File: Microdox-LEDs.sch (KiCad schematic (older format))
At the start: 33 parts, among them P1 USB, P2 CONN_01X03, SW0:0 SWITCH_DIODE, SW0:1 SWITCH_DIODE, SW0:2 SWITCH_DIODE, SW0:3 SWITCH_DIODE, SW0:4 SWITCH_DIODE, SW0:5 SWITCH_DIODE, SW0:6 SWITCH_DIODE, SW1:0 SWITCH_DIODE, SW1:1 SWITCH_DIODE, SW1:2 SWITCH_DIODE, SW1:3 SWITCH_DIODE, SW1:4 SWITCH_DIODE, SW1:5 SWITCH_DIODE, SW2:0 SWITCH_DIODE, SW2:1 SWITCH_DIODE, SW2:2 SWITCH_DIODE, SW2:3 SWITCH_DIODE, SW2:4 SWITCH_DIODE, SW2:5 SWITCH_DIODE, SW2:6 SWITCH_DIODE, SW3:0 SWITCH_DIODE, SW3:1 SWITCH_DIODE, SW3:2 SWITCH_DIODE, SW3:3 SWITCH_DIODE, SW3:4 SWITCH_DIODE, SW3:5 SWITCH_DIODE, SW3:6 SWITCH_DIODE, SW4:5 SWITCH_DIODE, SW4:6 SWITCH_DIODE

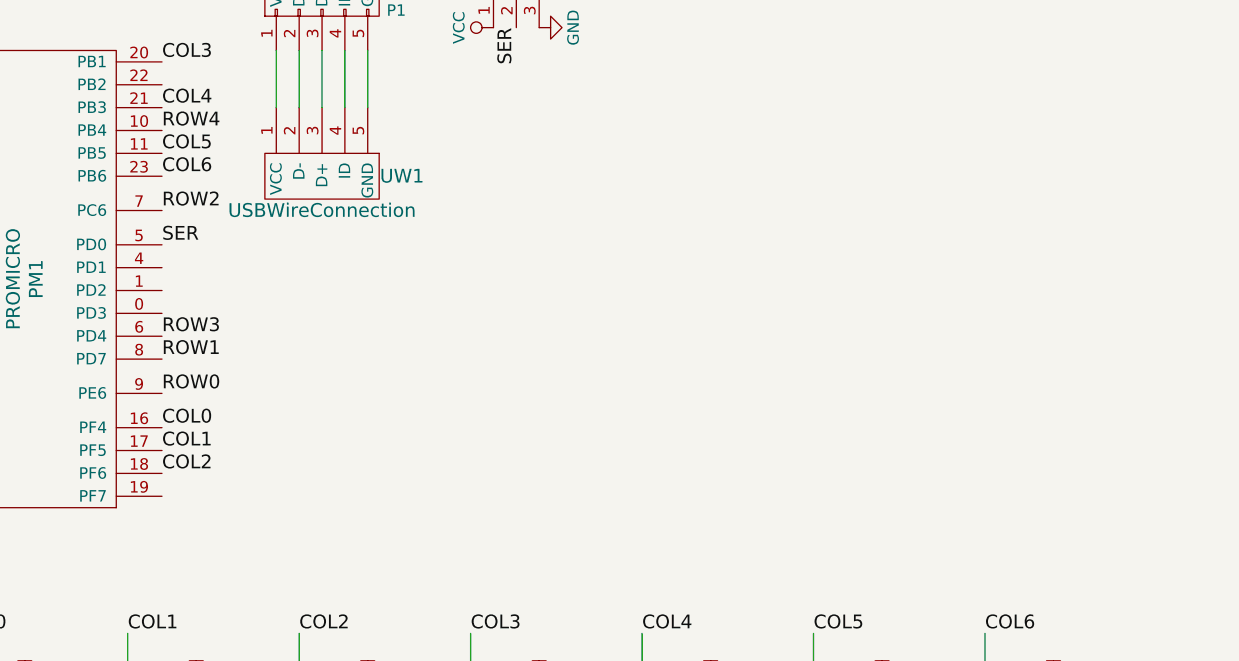
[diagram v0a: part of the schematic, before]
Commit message: Add version without backlighting
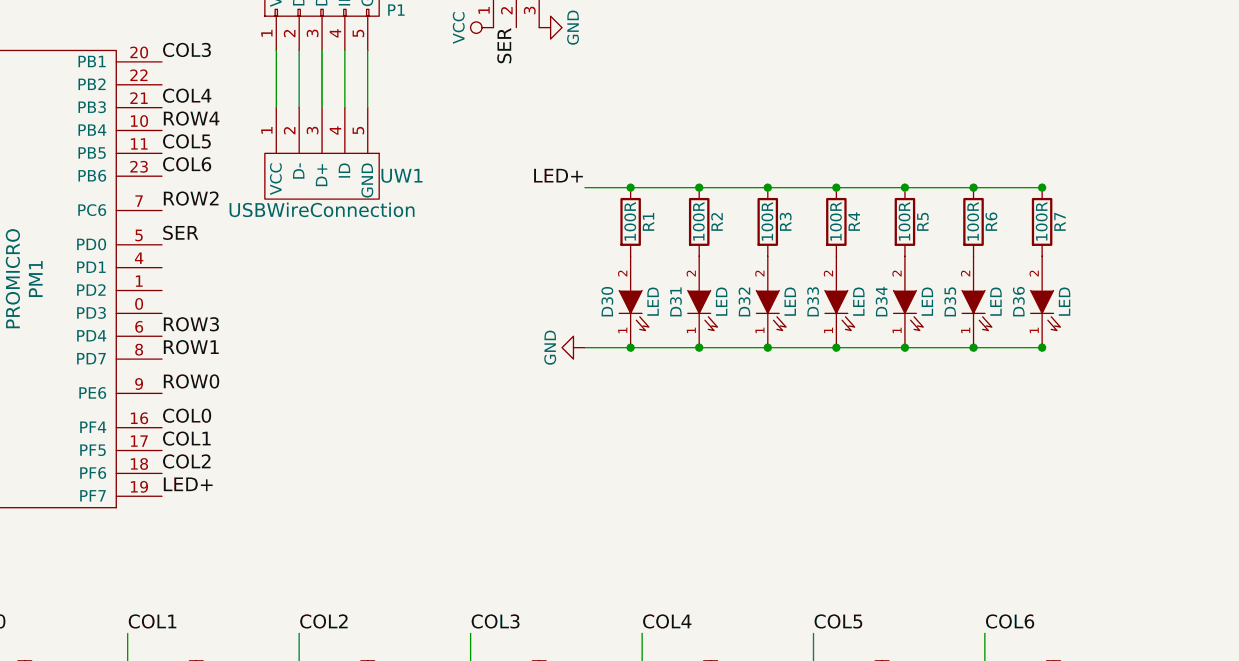
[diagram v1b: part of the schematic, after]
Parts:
- added D30, D31, D32, D33, D34, D35, D36: LED, LEDs:LED_1206, symbol LED
- added R1, R2, R3, R4, R5, R6, R7: 100R, Resistors_SMD:R_1206_HandSoldering, symbol R
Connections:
- net GND: now also D30.1 (K), D31.1 (K), D32.1 (K), D33.1 (K), D34.1 (K), D35.1 (K), D36.1 (K)
- net LED+: now reaches PM1.19 (PF7)
- net LED+: now also R1.1, R2.1, R3.1, R4.1, R5.1, R6.1, R7.1
- new net: D30.2 (A), R1.2
- new net: D31.2 (A), R2.2
- new net: D32.2 (A), R3.2
- new net: D33.2 (A), R4.2
- new net: D34.2 (A), R5.2
- new net: D35.2 (A), R6.2
- new net: D36.2 (A), R7.2
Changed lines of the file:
@@
 	1    0    0    -1
 $EndComp
+Text Label 2100 3450 0    60   ~ 0
+LED+
+Connection ~ 5050 2800
+Connection ~ 5650 2800
+Connection ~ 5950 2100
+Connection ~ 5650 2100
+Connection ~ 5350 2100
+Connection ~ 5050 2100
+Connection ~ 4750 2100
+Connection ~ 4450 2100
+Connection ~ 4150 2100
+Wire Wire Line
+	3950 2100 5950 2100
+Text Label 3950 2100 2    60   ~ 0
+LED+
+$Comp
+L GND #PWR07
+U 1 1 56F73DF4
+P 3950 2800
+F 0 "#PWR07" H 3950 2550 50  0001 C CNN
+F 1 "GND" H 3950 2650 50  0000 C CNN
+F 2 "" H 3950 2800 50  0000 C CNN
+F 3 "" H 3950 2800 50  0000 C CNN
+	1    3950 2800
+	0    1    1    0
+$EndComp
+Connection ~ 4150 2800
+Connection ~ 4450 2800
+Connection ~ 4750 2800
+Connection ~ 5350 2800
+$Comp
+L LED D34
+U 1 1 56F708E7
+P 5350 2600
+F 0 "D34" H 5350 2700 50  0000 C CNN
+F 1 "LED" H 5350 2500 50  0000 C CNN
+F 2 "LEDs:LED_1206" H 5350 2600 50  0001 C CNN
+F 3 "" H 5350 2600 50  0000 C CNN
+	1    5350 2600
+	0    -1   -1   0
+$EndComp
+$Comp
+L LED D33
+U 1 1 56F6ECAD
+P 5050 2600
+F 0 "D33" H 5050 2700 50  0000 C CNN
+F 1 "LED" H 5050 2500 50  0000 C CNN
+F 2 "LEDs:LED_1206" H 5050 2600 50  0001 C CNN
+F 3 "" H 5050 2600 50  0000 C CNN
+	1    5050 2600
+	0    -1   -1   0
+$EndComp
+$Comp
+L LED D32
+U 1 1 56F6EC9F
+P 4750 2600
+F 0 "D32" H 4750 2700 50  0000 C CNN
+F 1 "LED" H 4750 2500 50  0000 C CNN
+F 2 "LEDs:LED_1206" H 4750 2600 50  0001 C CNN
+F 3 "" H 4750 2600 50  0000 C CNN
+	1    4750 2600
+	0    -1   -1   0
+$EndComp
+$Comp
+L LED D31
+U 1 1 56F6D941
+P 4450 2600
+F 0 "D31" H 4450 2700 50  0000 C CNN
+F 1 "LED" H 4450 2500 50  0000 C CNN
+F 2 "LEDs:LED_1206" H 4450 2600 50  0001 C CNN
+F 3 "" H 4450 2600 50  0000 C CNN
+	1    4450 2600
+	0    -1   -1   0
+$EndComp
+$Comp
+L LED D30
+U 1 1 56F68FA0
+P 4150 2600
+F 0 "D30" H 4150 2700 50  0000 C CNN
+F 1 "LED" H 4150 2500 50  0000 C CNN
+F 2 "LEDs:LED_1206" H 4150 2600 50  0001 C CNN
+F 3 "" H 4150 2600 50  0000 C CNN
+	1    4150 2600
+	0    -1   -1   0
+$EndComp
+$Comp
+L R R1
+U 1 1 56F6BB88
+P 4150 2250
+F 0 "R1" V 4230 2250 50  0000 C CNN
+F 1 "100R" V 4150 2250 50  0000 C CNN
+F 2 "Resistors_SMD:R_1206_HandSoldering" V 4080 2250 50  0001 C CNN
+F 3 "" H 4150 2250 50  0000 C CNN
+	1    4150 2250
+	1    0    0    -1
+$EndComp
+$Comp
+L R R3
+U 1 1 56F6ECA5
+P 4750 2250
+F 0 "R3" V 4830 2250 50  0000 C CNN
+F 1 "100R" V 4750 2250 50  0000 C CNN
+F 2 "Resistors_SMD:R_1206_HandSoldering" V 4680 2250 50  0001 C CNN
+F 3 "" H 4750 2250 50  0000 C CNN
+	1    4750 2250
+	1    0    0    -1
+$EndComp
+$Comp
+L R R2
+U 1 1 56F6D947
+P 4450 2250
+F 0 "R2" V 4530 2250 50  0000 C CNN
+F 1 "100R" V 4450 2250 50  0000 C CNN
+F 2 "Resistors_SMD:R_1206_HandSoldering" V 4380 2250 50  0001 C CNN
+F 3 "" H 4450 2250 50  0000 C CNN
+	1    4450 2250
+	1    0    0    -1
+$EndComp
+$Comp
+L R R5
+U 1 1 56F708ED
+P 5350 2250
+F 0 "R5" V 5430 2250 50  0000 C CNN
+F 1 "100R" V 5350 2250 50  0000 C CNN
+F 2 "Resistors_SMD:R_1206_HandSoldering" V 5280 2250 50  0001 C CNN
+F 3 "" H 5350 2250 50  0000 C CNN
+	1    5350 2250
+	1    0    0    -1
+$EndComp
+$Comp
+L R R4
+U 1 1 56F6ECB3
+P 5050 2250
+F 0 "R4" V 5130 2250 50  0000 C CNN
+F 1 "100R" V 5050 2250 50  0000 C CNN
+F 2 "Resistors_SMD:R_1206_HandSoldering" V 4980 2250 50  0001 C CNN
+F 3 "" H 5050 2250 50  0000 C CNN
+	1    5050 2250
+	1    0    0    -1
+$EndComp
+$Comp
+L R R7
+U 1 1 56F70909
+P 5950 2250
+F 0 "R7" V 6030 2250 50  0000 C CNN
+F 1 "100R" V 5950 2250 50  0000 C CNN
+F 2 "Resistors_SMD:R_1206_HandSoldering" V 5880 2250 50  0001 C CNN
+F 3 "" H 5950 2250 50  0000 C CNN
+	1    5950 2250
+	1    0    0    -1
+$EndComp
+$Comp
+L R R6
+U 1 1 56F708FB
+P 5650 2250
+F 0 "R6" V 5730 2250 50  0000 C CNN
+F 1 "100R" V 5650 2250 50  0000 C CNN
+F 2 "Resistors_SMD:R_1206_HandSoldering" V 5580 2250 50  0001 C CNN
+F 3 "" H 5650 2250 50  0000 C CNN
+	1    5650 2250
+	1    0    0    -1
+$EndComp
+$Comp
+L LED D35
+U 1 1 56F708F5
+P 5650 2600
+F 0 "D35" H 5650 2700 50  0000 C CNN
+F 1 "LED" H 5650 2500 50  0000 C CNN
+F 2 "LEDs:LED_1206" H 5650 2600 50  0001 C CNN
+F 3 "" H 5650 2600 50  0000 C CNN
+	1    5650 2600
+	0    -1   -1   0
+$EndComp
+Wire Wire Line
+	3950 2800 5950 2800
+Connection ~ 5950 2800
+$Comp
+L LED D36
+U 1 1 56F70903
+P 5950 2600
+F 0 "D36" H 5950 2700 50  0000 C CNN
+F 1 "LED" H 5950 2500 50  0000 C CNN
+F 2 "LEDs:LED_1206" H 5950 2600 50  0001 C CNN
+F 3 "" H 5950 2600 50  0000 C CNN
+	1    5950 2600
+	0    -1   -1   0
+$EndComp
 $EndSCHEMATC
